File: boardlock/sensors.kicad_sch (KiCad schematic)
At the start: 21 parts, among them Q2 MMBT4401, Q4 BSS84PWH6327XTSA1, U1 LSM6DSO32, U3 SAM-M8Q

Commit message: more pcb stuff
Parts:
- renumbered C22 to C5, R28 to R14, R25 to R7, TP21 to TP39, TP1 to TP40, TP3 to TP41, TP2 to TP42
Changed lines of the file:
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@@
   (symbol (lib_id "Device:C_Small") (at 276.86 128.27 0) (unit 1)
     (in_bom yes) (on_board yes) (dnp no) (fields_autoplaced)
-    (property "Reference" "C22" (at 279.4 127.0063 0)
+    (property "Reference" "C5" (at 279.4 127.0063 0)
       (effects (font (size 1.27 1.27)) (justify left))
     )
@@
       (project "boardlock"
         (path "/e1fc29ce-837e-4062-84d8-c7e423f9eab9/a4a6f965-a4d9-4da6-b64e-79eda0daabe5"
-          (reference "C22") (unit 1)
+          (reference "C5") (unit 1)
         )
       )
@@
   (symbol (lib_id "Connector:TestPoint") (at 199.39 121.92 90) (unit 1)
     (in_bom yes) (on_board yes) (dnp no)
-    (property "Reference" "TP3" (at 179.07 121.92 90)
+    (property "Reference" "TP41" (at 179.07 121.92 90)
       (effects (font (size 1.27 1.27)))
     )
@@
       (project "boardlock"
         (path "/e1fc29ce-837e-4062-84d8-c7e423f9eab9/a4a6f965-a4d9-4da6-b64e-79eda0daabe5"
-          (reference "TP3") (unit 1)
+          (reference "TP41") (unit 1)
         )
       )
@@
       (project "boardlock"
         (path "/e1fc29ce-837e-4062-84d8-c7e423f9eab9/a4a6f965-a4d9-4da6-b64e-79eda0daabe5"
-          (reference "#PWR05") (unit 1)
+          (reference "#PWR07") (unit 1)
         )
       )
@@
   (symbol (lib_id "Connector:TestPoint") (at 199.39 119.38 90) (unit 1)
     (in_bom yes) (on_board yes) (dnp no)
-    (property "Reference" "TP1" (at 181.61 119.38 90)
+    (property "Reference" "TP40" (at 181.61 119.38 90)
       (effects (font (size 1.27 1.27)))
     )
@@
       (project "boardlock"
         (path "/e1fc29ce-837e-4062-84d8-c7e423f9eab9/a4a6f965-a4d9-4da6-b64e-79eda0daabe5"
-          (reference "TP1") (unit 1)
+          (reference "TP40") (unit 1)
         )
       )
@@
       (project "boardlock"
         (path "/e1fc29ce-837e-4062-84d8-c7e423f9eab9/a4a6f965-a4d9-4da6-b64e-79eda0daabe5"
-          (reference "#PWR011") (unit 1)
+          (reference "#PWR09") (unit 1)
         )
       )
@@
       (project "boardlock"
         (path "/e1fc29ce-837e-4062-84d8-c7e423f9eab9/a4a6f965-a4d9-4da6-b64e-79eda0daabe5"
-          (reference "#PWR07") (unit 1)
+          (reference "#PWR010") (unit 1)
         )
       )
@@
   (symbol (lib_id "Connector:TestPoint") (at 199.39 124.46 90) (unit 1)
     (in_bom yes) (on_board yes) (dnp no)
-    (property "Reference" "TP2" (at 179.07 124.46 90)
+    (property "Reference" "TP42" (at 179.07 124.46 90)
       (effects (font (size 1.27 1.27)))
     )
@@
       (project "boardlock"
         (path "/e1fc29ce-837e-4062-84d8-c7e423f9eab9/a4a6f965-a4d9-4da6-b64e-79eda0daabe5"
-          (reference "TP2") (unit 1)
+          (reference "TP42") (unit 1)
         )
       )
@@
   (symbol (lib_id "Connector:TestPoint") (at 102.87 68.58 270) (unit 1)
     (in_bom yes) (on_board yes) (dnp no)
-    (property "Reference" "TP21" (at 120.65 68.58 90)
+    (property "Reference" "TP39" (at 120.65 68.58 90)
       (effects (font (size 1.27 1.27)))
     )
@@
       (project "boardlock"
         (path "/e1fc29ce-837e-4062-84d8-c7e423f9eab9/a4a6f965-a4d9-4da6-b64e-79eda0daabe5"
-          (reference "TP21") (unit 1)
+          (reference "TP39") (unit 1)
         )
       )
@@
   (symbol (lib_id "Device:R_US") (at 228.6 154.94 0) (unit 1)
     (in_bom yes) (on_board yes) (dnp no) (fields_autoplaced)
-    (property "Reference" "R28" (at 231.14 153.67 0)
+    (property "Reference" "R14" (at 231.14 153.67 0)
       (effects (font (size 1.27 1.27)) (justify left))
     )
@@
       (project "boardlock"
         (path "/e1fc29ce-837e-4062-84d8-c7e423f9eab9/a4a6f965-a4d9-4da6-b64e-79eda0daabe5"
-          (reference "R28") (unit 1)
+          (reference "R14") (unit 1)
         )
       )
@@
       (project "boardlock"
         (path "/e1fc29ce-837e-4062-84d8-c7e423f9eab9/a4a6f965-a4d9-4da6-b64e-79eda0daabe5"
-          (reference "R15") (unit 1)
+          (reference "R11") (unit 1)
         )
       )
@@
       (project "boardlock"
         (path "/e1fc29ce-837e-4062-84d8-c7e423f9eab9/a4a6f965-a4d9-4da6-b64e-79eda0daabe5"
-          (reference "R6") (unit 1)
+          (reference "R5") (unit 1)
         )
       )
@@
       (project "boardlock"
         (path "/e1fc29ce-837e-4062-84d8-c7e423f9eab9/a4a6f965-a4d9-4da6-b64e-79eda0daabe5"
-          (reference "#PWR010") (unit 1)
+          (reference "#PWR06") (unit 1)
         )
       )
@@
       (project "boardlock"
         (path "/e1fc29ce-837e-4062-84d8-c7e423f9eab9/a4a6f965-a4d9-4da6-b64e-79eda0daabe5"
-          (reference "Q4") (unit 1)
+          (reference "Q1") (unit 1)
         )
       )
@@
       (project "boardlock"
         (path "/e1fc29ce-837e-4062-84d8-c7e423f9eab9/a4a6f965-a4d9-4da6-b64e-79eda0daabe5"
-          (reference "#PWR062") (unit 1)
+          (reference "#PWR014") (unit 1)
         )
       )
@@
   (symbol (lib_id "Device:R_US") (at 181.61 63.5 0) (unit 1)
     (in_bom yes) (on_board yes) (dnp no) (fields_autoplaced)
-    (property "Reference" "R25" (at 184.15 62.23 0)
+    (property "Reference" "R7" (at 184.15 62.23 0)
       (effects (font (size 1.27 1.27)) (justify left))
     )
@@
       (project "boardlock"
         (path "/e1fc29ce-837e-4062-84d8-c7e423f9eab9/a4a6f965-a4d9-4da6-b64e-79eda0daabe5"
-          (reference "R25") (unit 1)
+          (reference "R7") (unit 1)
         )
       )
@@
       (project "boardlock"
         (path "/e1fc29ce-837e-4062-84d8-c7e423f9eab9/a4a6f965-a4d9-4da6-b64e-79eda0daabe5"
-          (reference "#PWR09") (unit 1)
+          (reference "#PWR012") (unit 1)
         )
       )
@@
       (project "boardlock"
         (path "/e1fc29ce-837e-4062-84d8-c7e423f9eab9/a4a6f965-a4d9-4da6-b64e-79eda0daabe5"
-          (reference "Q3") (unit 1)
+          (reference "Q2") (unit 1)
         )
       )
@@
       (project "boardlock"
         (path "/e1fc29ce-837e-4062-84d8-c7e423f9eab9/a4a6f965-a4d9-4da6-b64e-79eda0daabe5"
-          (reference "R5") (unit 1)
+          (reference "R6") (unit 1)
         )
       )
@@
       (project "boardlock"
         (path "/e1fc29ce-837e-4062-84d8-c7e423f9eab9/a4a6f965-a4d9-4da6-b64e-79eda0daabe5"
-          (reference "#PWR012") (unit 1)
+          (reference "#PWR015") (unit 1)
         )
       )
@@
       (project "boardlock"
         (path "/e1fc29ce-837e-4062-84d8-c7e423f9eab9/a4a6f965-a4d9-4da6-b64e-79eda0daabe5"
-          (reference "R7") (unit 1)
+          (reference "R12") (unit 1)
         )
       )
@@
       (project "boardlock"
         (path "/e1fc29ce-837e-4062-84d8-c7e423f9eab9/a4a6f965-a4d9-4da6-b64e-79eda0daabe5"
-          (reference "R2") (unit 1)
+          (reference "R8") (unit 1)
         )
       )
@@
   (symbol (lib_id "power:+3V3") (at 228.6 147.32 0) (unit 1)
     (in_bom yes) (on_board yes) (dnp no) (fields_autoplaced)
-    (property "Reference" "#PWR084" (at 228.6 151.13 0)
+    (property "Reference" "#PWR016" (at 228.6 151.13 0)
       (effects (font (size 1.27 1.27)) hide)
     )
@@
       (project "boardlock"
         (path "/e1fc29ce-837e-4062-84d8-c7e423f9eab9/a4a6f965-a4d9-4da6-b64e-79eda0daabe5"
-          (reference "#PWR084") (unit 1)
+          (reference "#PWR016") (unit 1)
         )
       )
@@
       (project "boardlock"
         (path "/e1fc29ce-837e-4062-84d8-c7e423f9eab9/a4a6f965-a4d9-4da6-b64e-79eda0daabe5"
-          (reference "R3") (unit 1)
+          (reference "R9") (unit 1)
         )
       )
@@
       (project "boardlock"
         (path "/e1fc29ce-837e-4062-84d8-c7e423f9eab9/a4a6f965-a4d9-4da6-b64e-79eda0daabe5"
-          (reference "#PWR04") (unit 1)
+          (reference "#PWR08") (unit 1)
         )
       )
@@
       (project "boardlock"
         (path "/e1fc29ce-837e-4062-84d8-c7e423f9eab9/a4a6f965-a4d9-4da6-b64e-79eda0daabe5"
-          (reference "#PWR059") (unit 1)
+          (reference "#PWR011") (unit 1)
         )
       )
@@
       (project "boardlock"
         (path "/e1fc29ce-837e-4062-84d8-c7e423f9eab9/a4a6f965-a4d9-4da6-b64e-79eda0daabe5"
-          (reference "R1") (unit 1)
+          (reference "R10") (unit 1)
         )
       )
@@
       (project "boardlock"
         (path "/e1fc29ce-837e-4062-84d8-c7e423f9eab9/a4a6f965-a4d9-4da6-b64e-79eda0daabe5"
-          (reference "R8") (unit 1)
+          (reference "R13") (unit 1)
         )
       )
@@
       (project "boardlock"
         (path "/e1fc29ce-837e-4062-84d8-c7e423f9eab9/a4a6f965-a4d9-4da6-b64e-79eda0daabe5"
-          (reference "#PWR061") (unit 1)
-        )
-      )
+          (reference "#PWR013") (unit 1)
+        )
+      )

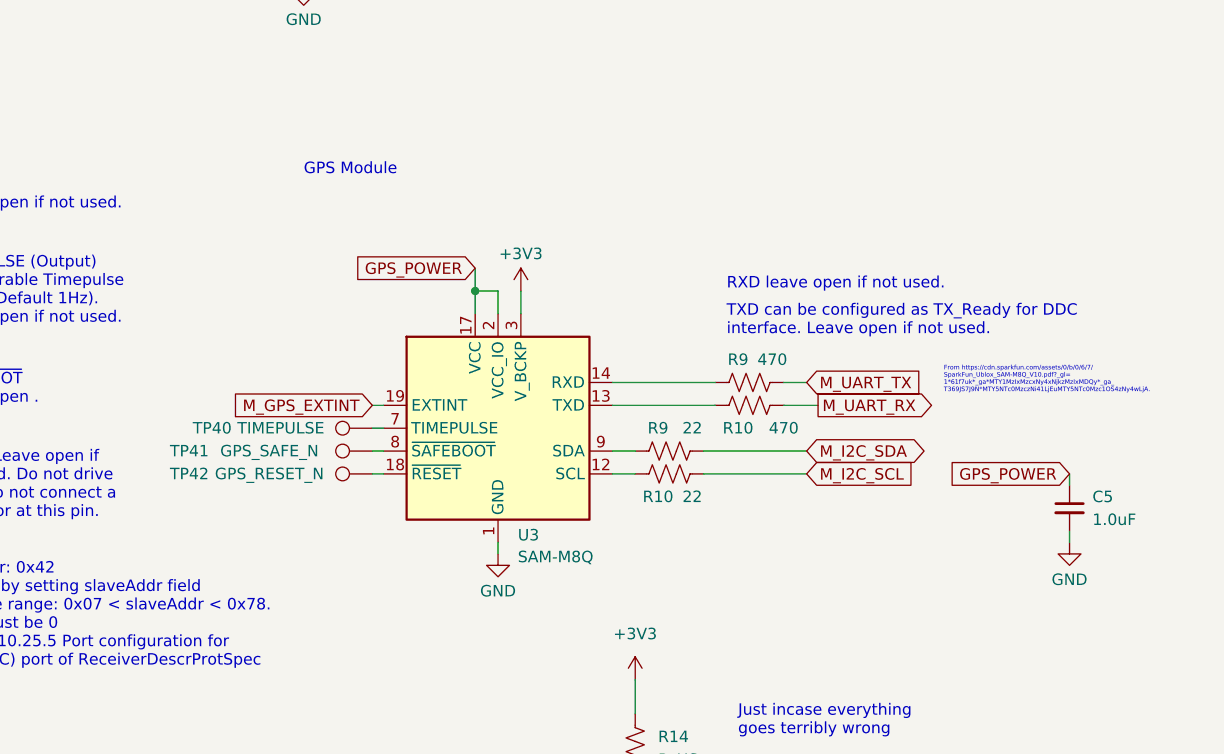
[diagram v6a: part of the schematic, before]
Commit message: updating gps caps
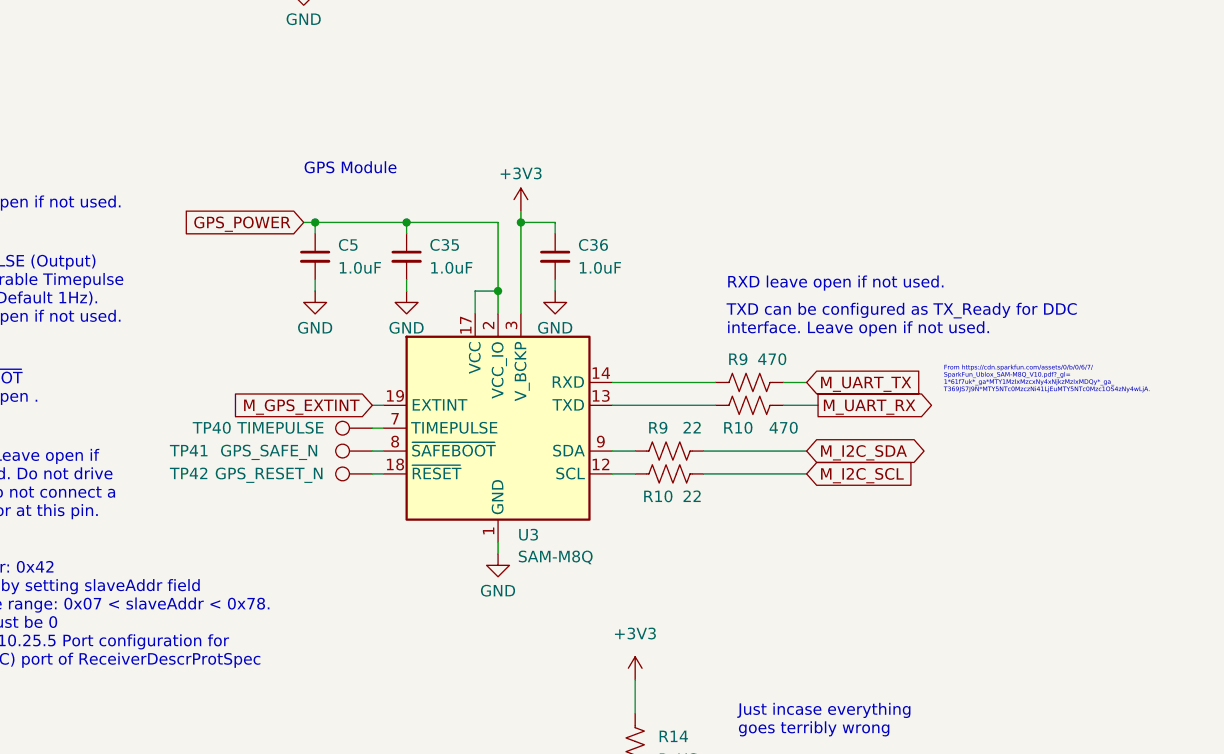
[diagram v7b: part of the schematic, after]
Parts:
- added C35, C36: 1.0uF, Capacitor_SMD:C_0805_2012Metric_Pad1.18x1.45mm_HandSolder, symbol Device:C_Small
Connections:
- net +3V3: now also C36.1
- net GND: now also C35.2, C36.2
- net GPS_POWER: now also C35.1

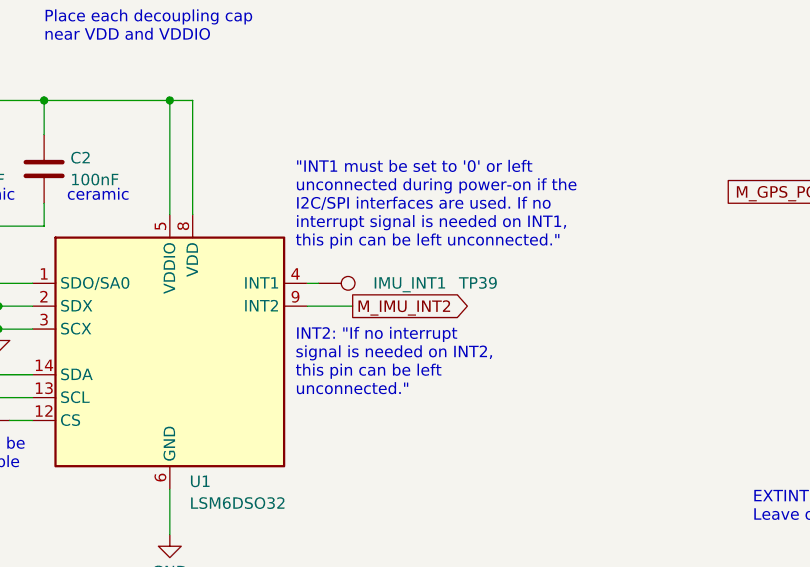
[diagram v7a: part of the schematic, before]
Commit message: making 3.3 bigger and deleting testpoints
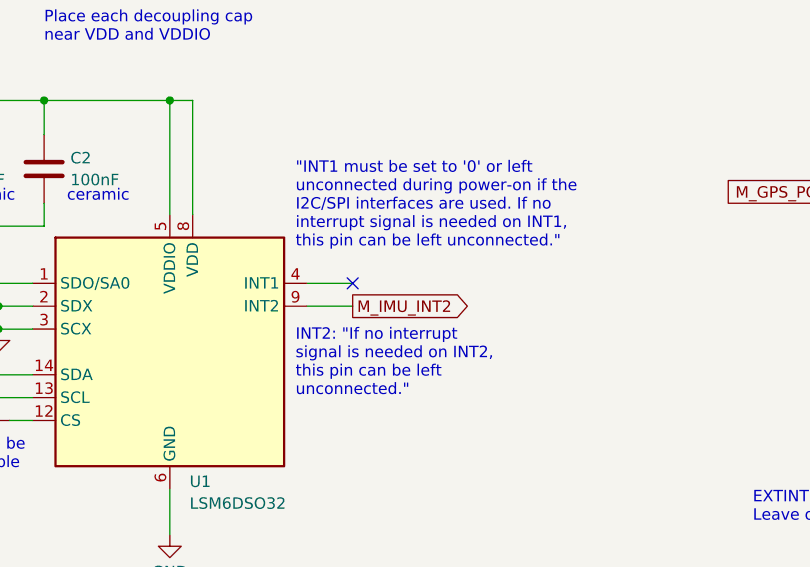
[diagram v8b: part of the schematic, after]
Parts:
- removed TP39: IMU_INT1, TestPoint:TestPoint_Pad_D1.0mm, symbol Connector:TestPoint
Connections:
- no-connect marks 0 -> 1
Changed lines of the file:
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@@
   (junction (at 59.69 62.23) (diameter 0) (color 0 0 0 0)
   )
+  (no_connect (at 106.68 68.58))
   (wire (pts (xy 199.39 116.84) (xy 200.66 116.84))
     (stroke (width 0) (type default))
@@
     (stroke (width 0) (type default))
   )
-  (wire (pts (xy 101.6 68.58) (xy 102.87 68.58))
+  (wire (pts (xy 101.6 68.58) (xy 106.68 68.58))
     (stroke (width 0) (type default))
   )
@@
         )
       )
-    )
-  )
-  (symbol (lib_id "Connector:TestPoint") (at 102.87 68.58 270) (unit 1)
-    (in_bom yes) (on_board yes) (dnp no)
-    (property "Reference" "TP39" (at 120.65 68.58 90)
-      (effects (font (size 1.27 1.27)))
-    )
-    (property "Value" "IMU_INT1" (at 113.03 68.58 90)
-      (effects (font (size 1.27 1.27)))
-    )
-    (property "Footprint" "TestPoint:TestPoint_Pad_D1.0mm" (at 102.87 73.66 0)
-      (effects (font (size 1.27 1.27)) hide)
-    )
-    (property "Datasheet" "~" (at 102.87 73.66 0)
-      (effects (font (size 1.27 1.27)) hide)
-    )
-    (pin "1")
-    (instances
-      (project "boardlock"
-        (path "/e1fc29ce-837e-4062-84d8-c7e423f9eab9/a4a6f965-a4d9-4da6-b64e-79eda0daabe5"
-          (reference "TP39") (unit 1)
-        )
-      )
